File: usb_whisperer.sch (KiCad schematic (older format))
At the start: 1 part, among them J1 Conn_01x04

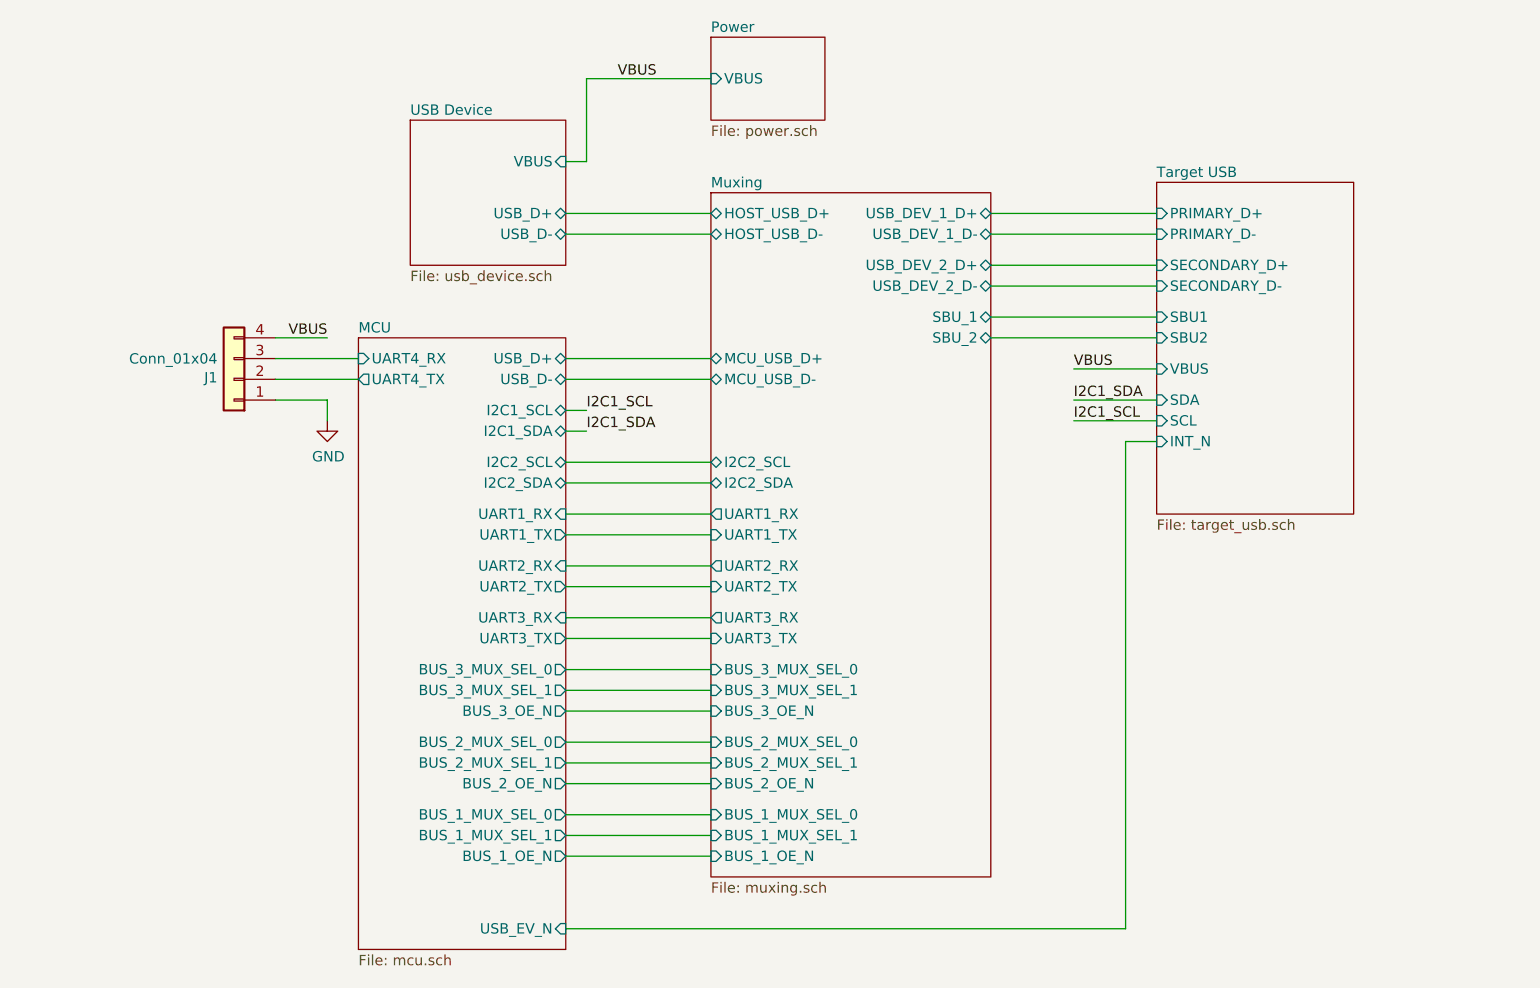
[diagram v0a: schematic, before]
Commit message: Complete muxing and level translation
Added Aux USB to avoid using a HUB, which don't seem to be too readily
available out there and would complicate the design for no good reason.

Now the i2c lines can also be switched.

Added voltage level translation up to 1.2V from 3.3V. Selected
bidirectional level translator.

Started looking into power supply.
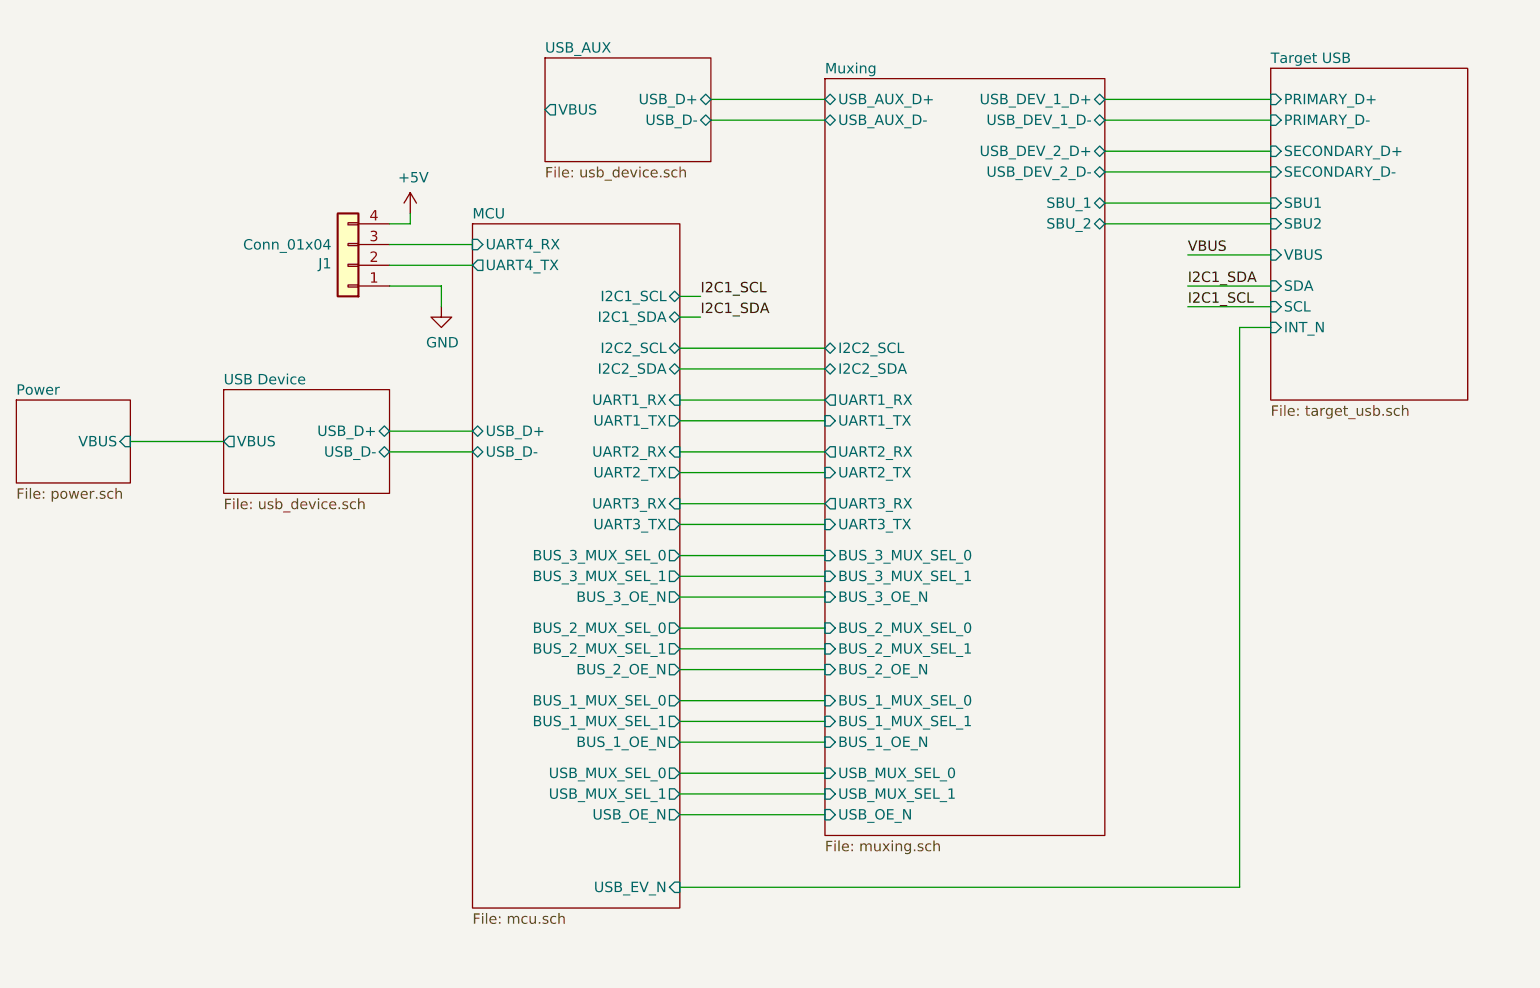
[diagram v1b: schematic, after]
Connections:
- net VBUS: no longer J1.4 (Pin_4)
- new net +5V: J1.4 (Pin_4)
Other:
- moved on the sheet: J1

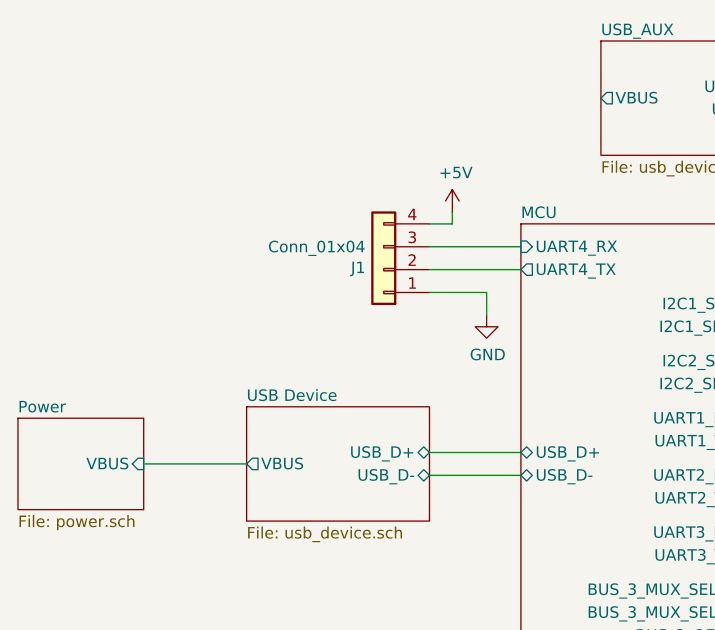
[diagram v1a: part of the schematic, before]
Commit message: Add initial power design
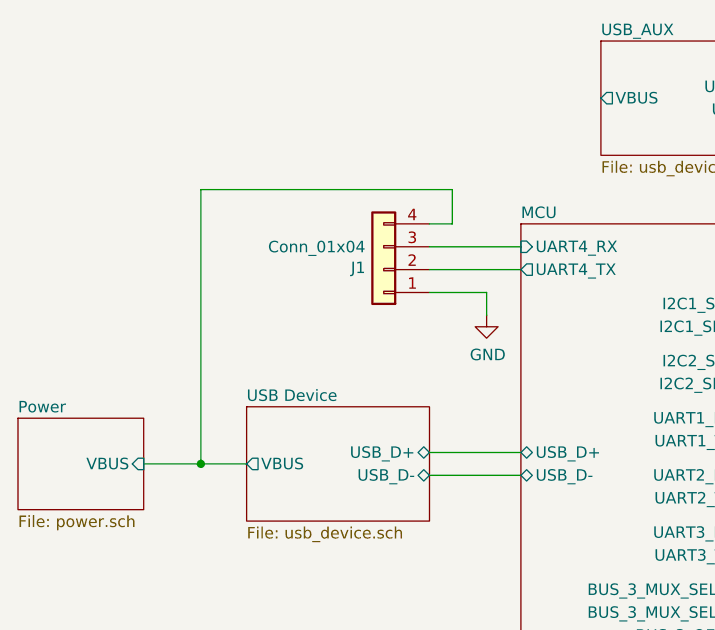
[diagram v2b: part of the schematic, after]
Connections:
- net +5V is gone; now on net Power/VBUS: J1.4 (Pin_4)
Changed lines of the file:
@@
 $EndSheet
 Wire Wire Line
-	3000 3950 2550 3950
+	3000 3950 2800 3950
 Wire Wire Line
 	3800 3900 4200 3900
@@
 Wire Wire Line
 	5200 5750 5900 5750
-$Comp
-L power:+5V #PWR?
-U 1 1 61C230FC
-P 3900 2850
-F 0 "#PWR?" H 3900 2700 50  0001 C CNN
-F 1 "+5V" H 3915 3023 50  0000 C CNN
-F 2 "" H 3900 2850 50  0001 C CNN
-F 3 "" H 3900 2850 50  0001 C CNN
-	1    3900 2850
-	1    0    0    -1
-$EndComp
-Wire Wire Line
-	3900 2850 3900 2900
 Wire Wire Line
 	3900 2900 3800 2900
+Wire Wire Line
+	3900 2750 2800 2750
+Wire Wire Line
+	2800 2750 2800 3950
+Wire Wire Line
+	3900 2750 3900 2900
+Connection ~ 2800 3950
+Wire Wire Line
+	2800 3950 2550 3950
 $EndSCHEMATC

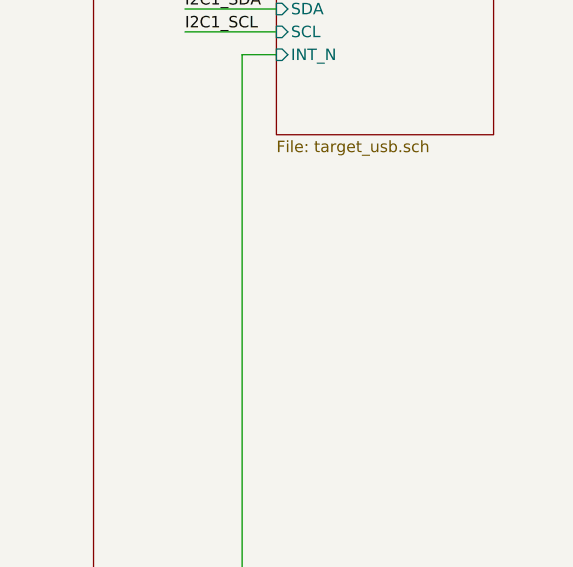
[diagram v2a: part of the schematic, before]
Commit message: Supply caps, initial signal states and headers
  * Added bulk supply caps.
  * Set initial control signal states via resistors.
  * Add debug headers.
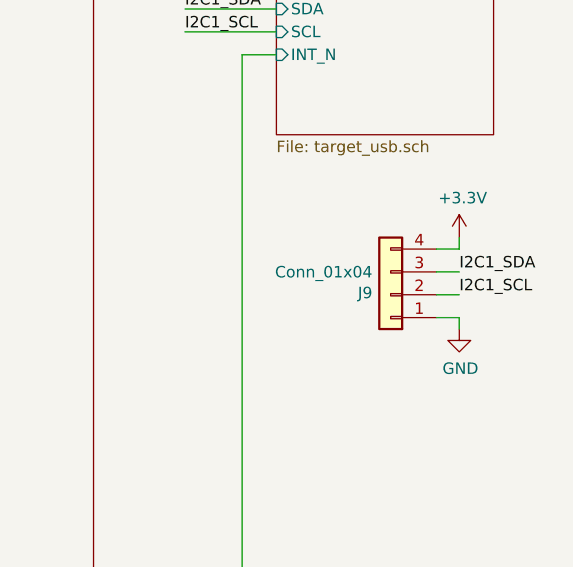
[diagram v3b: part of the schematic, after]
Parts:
- added J9: Conn_01x04, symbol Connector_Generic:Conn_01x04
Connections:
- net GND: now also J9.1 (Pin_1)
- net I2C1_SCL: now also J9.2 (Pin_2)
- net I2C1_SDA: now also J9.3 (Pin_3)
- new net +3V3: J9.4 (Pin_4)
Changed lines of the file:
@@
 Wire Wire Line
 	2800 3950 2550 3950
+$Comp
+L Connector_Generic:Conn_01x04 J9
+U 1 1 61A82B7E
+P 8550 4450
+F 0 "J9" H 8630 4442 50  0000 L CNN
+F 1 "Conn_01x04" H 8630 4351 50  0000 L CNN
+F 2 "" H 8550 4450 50  0001 C CNN
+F 3 "~" H 8550 4450 50  0001 C CNN
+	1    8550 4450
+	-1   0    0    1
+$EndComp
+Text Label 8850 4350 0    50   ~ 0
+I2C1_SDA
+Text Label 8850 4450 0    50   ~ 0
+I2C1_SCL
+Wire Wire Line
+	8750 4350 8850 4350
+Wire Wire Line
+	8850 4450 8750 4450
+$Comp
+L power:+3.3V #PWR010
+U 1 1 61A89DD5
+P 8850 4200
+F 0 "#PWR010" H 8850 4050 50  0001 C CNN
+F 1 "+3.3V" H 8865 4373 50  0000 C CNN
+F 2 "" H 8850 4200 50  0001 C CNN
+F 3 "" H 8850 4200 50  0001 C CNN
+	1    8850 4200
+	1    0    0    -1
+$EndComp
+$Comp
+L power:GND #PWR017
+U 1 1 61A8BB25
+P 8850 4600
+F 0 "#PWR017" H 8850 4350 50  0001 C CNN
+F 1 "GND" H 8855 4427 50  0000 C CNN
+F 2 "" H 8850 4600 50  0001 C CNN
+F 3 "" H 8850 4600 50  0001 C CNN
+	1    8850 4600
+	1    0    0    -1
+$EndComp
+Wire Wire Line
+	8850 4200 8850 4250
+Wire Wire Line
+	8850 4250 8750 4250
+Wire Wire Line
+	8750 4550 8850 4550
+Wire Wire Line
+	8850 4550 8850 4600
 $EndSCHEMATC
